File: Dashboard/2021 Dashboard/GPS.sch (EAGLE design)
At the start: 1 part

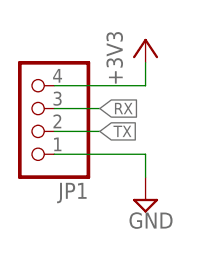
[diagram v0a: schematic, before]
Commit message: More work done to dash hub and dial, gps board added
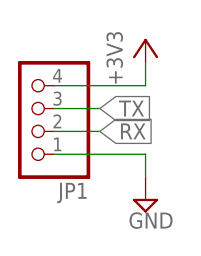
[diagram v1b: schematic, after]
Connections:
- net RX: now also JP1.2; no longer JP1.3
- net TX: now also JP1.3; no longer JP1.2
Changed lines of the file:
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@@
 </busses>
 <nets>
-<net name="RX" class="0">
-<segment>
-<pinref part="JP1" gate="A" pin="3"/>
-<wire x1="33.02" y1="45.72" x2="38.1" y2="45.72" width="0.1524" layer="91"/>
-<label x="38.1" y="45.72" size="1.27" layer="95" xref="yes"/>
-</segment>
-</net>
-<net name="TX" class="0">
-<segment>
-<pinref part="JP1" gate="A" pin="2"/>
-<wire x1="33.02" y1="43.18" x2="38.1" y2="43.18" width="0.1524" layer="91"/>
-<label x="38.1" y="43.18" size="1.27" layer="95" xref="yes"/>
-</segment>
-</net>
 <net name="GND" class="0">
 <segment>
@@
 </segment>
 </net>
+<net name="TX" class="0">
+<segment>
+<pinref part="JP1" gate="A" pin="3"/>
+<wire x1="33.02" y1="45.72" x2="38.1" y2="45.72" width="0.1524" layer="91"/>
+<label x="38.1" y="45.72" size="1.778" layer="95" xref="yes"/>
+</segment>
+</net>
+<net name="RX" class="0">
+<segment>
+<pinref part="JP1" gate="A" pin="2"/>
+<wire x1="38.1" y1="43.18" x2="33.02" y2="43.18" width="0.1524" layer="91"/>
+<label x="38.1" y="43.18" size="1.778" layer="95" xref="yes"/>
+</segment>
+</net>
